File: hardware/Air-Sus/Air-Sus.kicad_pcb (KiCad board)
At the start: 2 copper layers, 1 part, among them U1 BME280

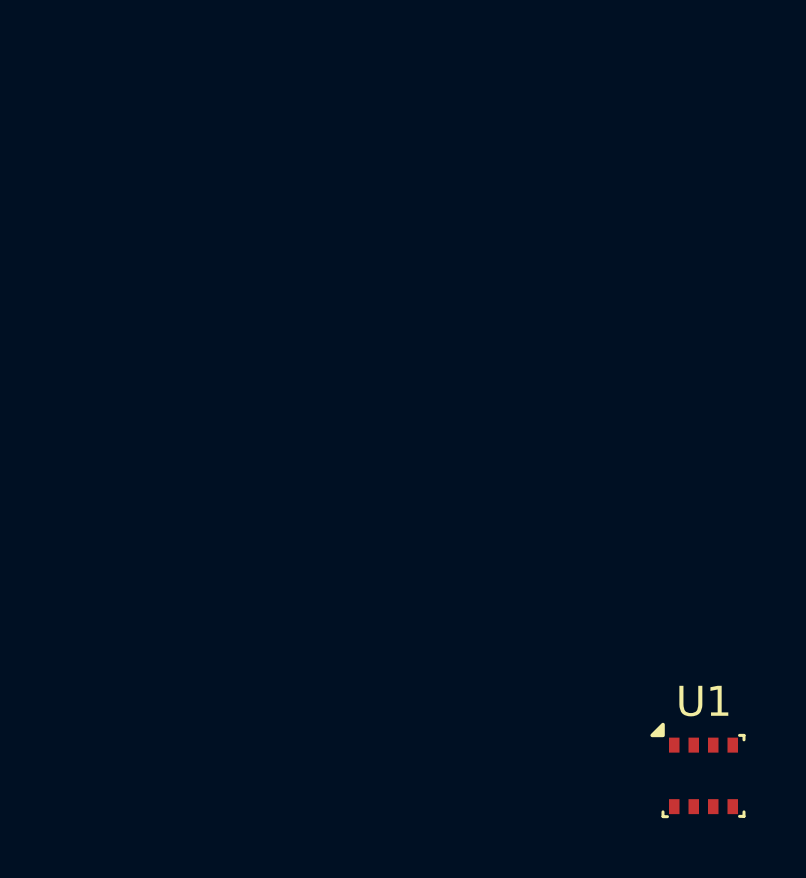
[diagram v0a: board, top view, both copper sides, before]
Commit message: added op-amp, finished footprints, new connector, fuse, ldo
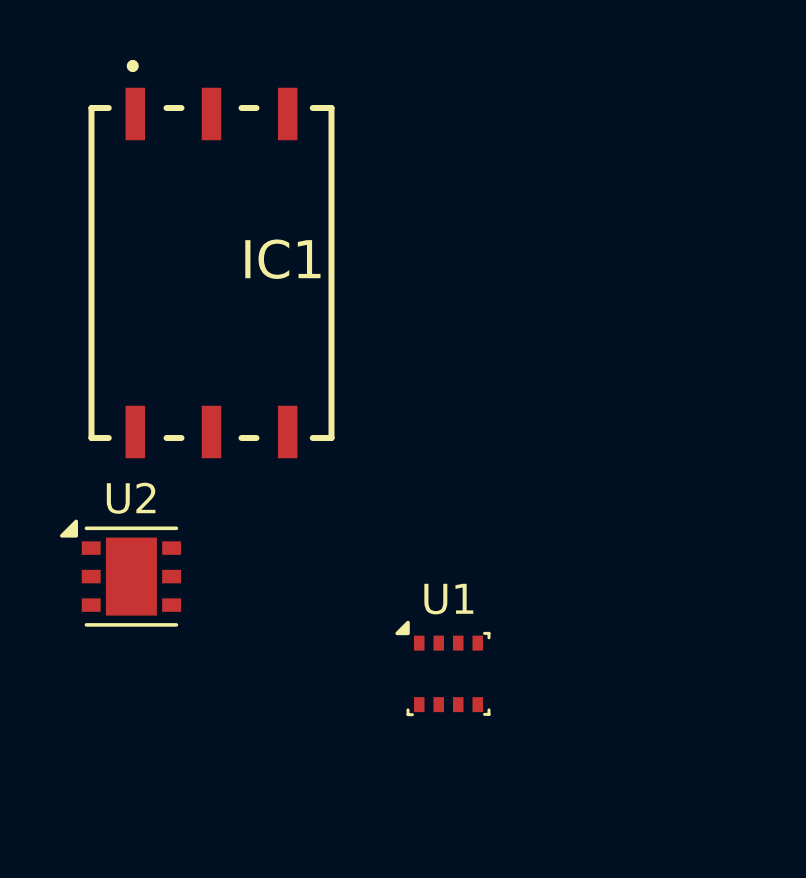
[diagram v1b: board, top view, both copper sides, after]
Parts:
- added IC1: ABPMRRV060MG2A3, footprints:ABPMRRV060MG2A3, F.Cu at (103.0, 69.6)
- added U2: LDO40LPURY, Package_DFN_QFN:DFN-6-1EP_3x3mm_P0.95mm_EP1.7x2.6mm, F.Cu at (100.4, 79.7)
- moved U1 9.15 mm to (110.9, 83.0)

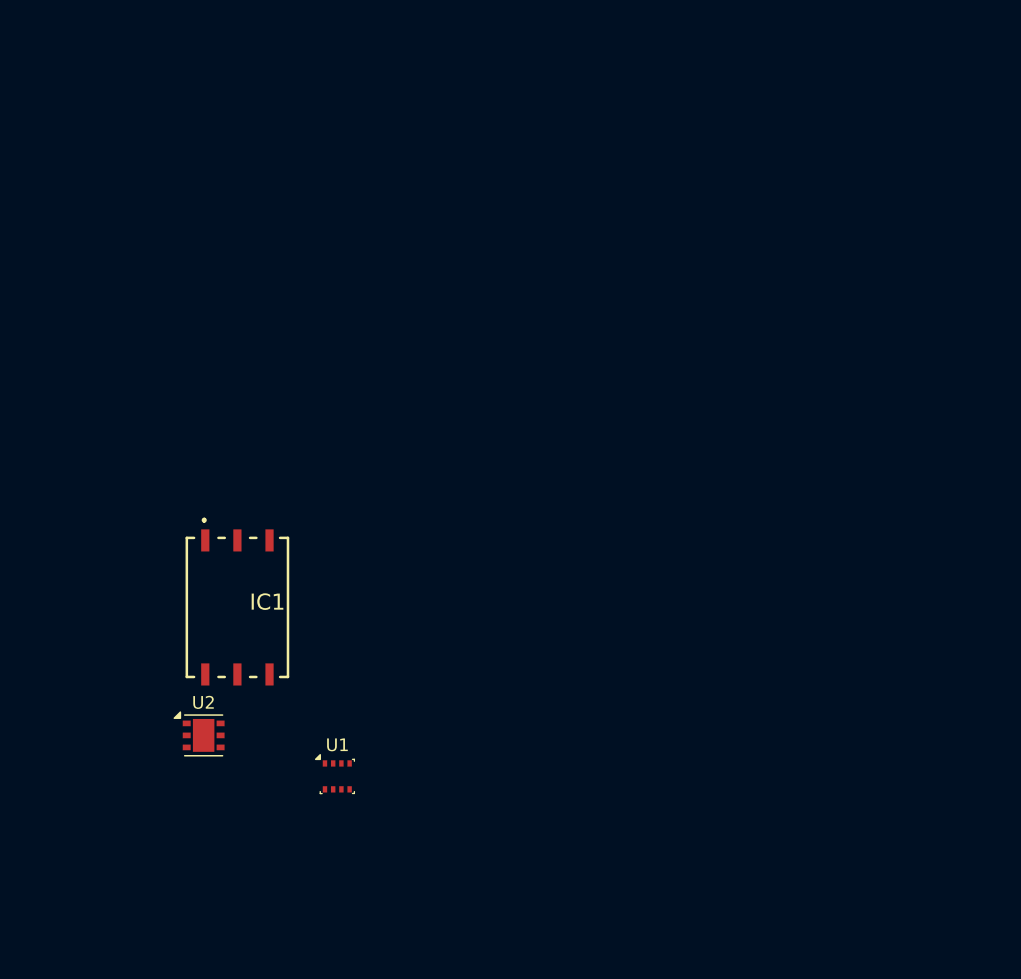
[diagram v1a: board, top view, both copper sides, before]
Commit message: added configurable options for board type/connector, cubemx ioc, nanofit for ir rideheight, added part numbers, etc.
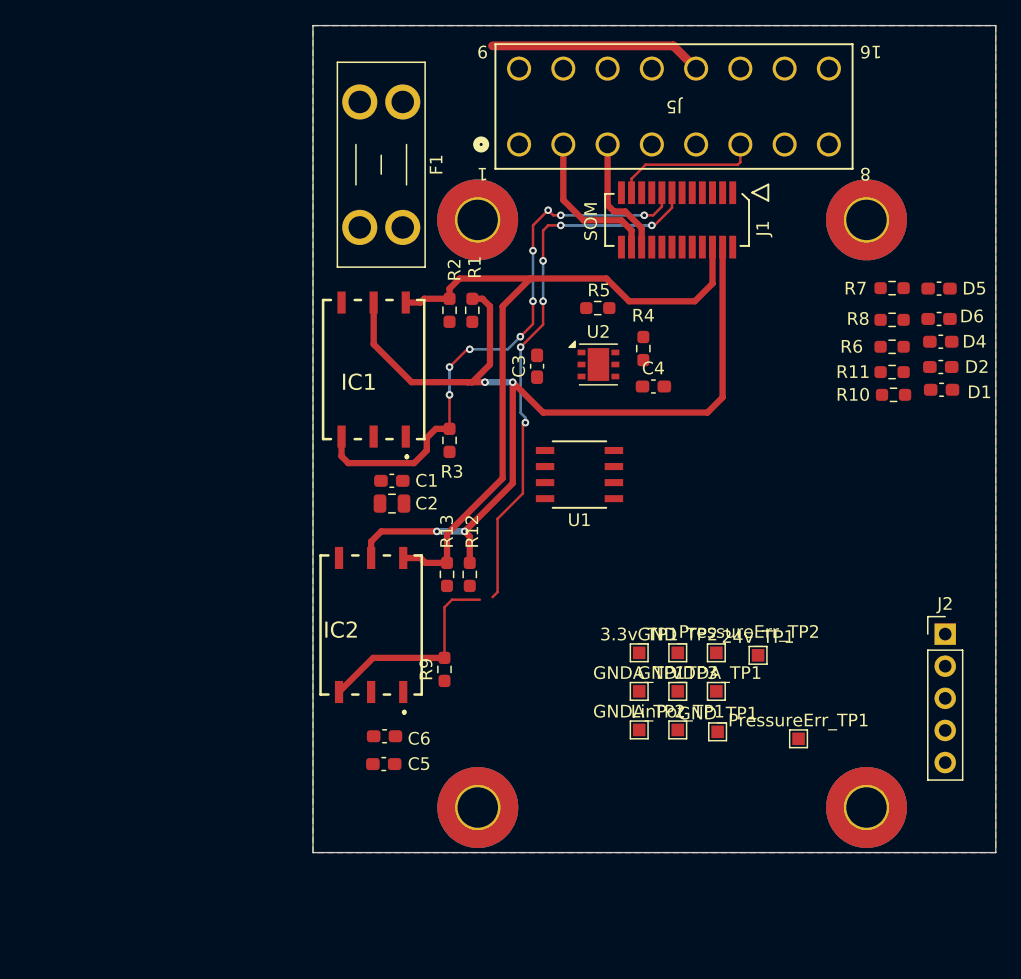
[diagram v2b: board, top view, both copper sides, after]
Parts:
- added 24v_TP1: TestPoint, TestPoint:TestPoint_Pad_1.0x1.0mm, F.Cu at (144.2, 73.4)
- added 3.3v_TP1: TestPoint, TestPoint:TestPoint_Pad_1.0x1.0mm, F.Cu at (134.8, 73.2)
- added C1: 0.1uF, Capacitor_SMD:C_0603_1608Metric_Pad1.08x0.95mm_HandSolder, F.Cu at (115.2, 59.6)
- added C2: 10uf, Capacitor_SMD:C_0805_2012Metric, F.Cu at (115.2, 61.4)
- added C3: 1uF, Capacitor_SMD:C_0603_1608Metric_Pad1.08x0.95mm_HandSolder, F.Cu at (126.7, 50.5)
- added C4: 1uF, Capacitor_SMD:C_0603_1608Metric_Pad1.08x0.95mm_HandSolder, F.Cu at (135.9, 52.1)
- added C5: 10uf, Capacitor_SMD:C_0603_1608Metric_Pad1.08x0.95mm_HandSolder, F.Cu at (114.6, 82.0)
- added C6: 0.1uF, Capacitor_SMD:C_0603_1608Metric_Pad1.08x0.95mm_HandSolder, F.Cu at (114.7, 79.8)
- added D1: LED, Capacitor_SMD:C_0603_1608Metric_Pad1.08x0.95mm_HandSolder, F.Cu at (158.7, 52.4)
- added D2: LED, Capacitor_SMD:C_0603_1608Metric_Pad1.08x0.95mm_HandSolder, F.Cu at (158.7, 50.6)
- added D4: LED, Capacitor_SMD:C_0603_1608Metric_Pad1.08x0.95mm_HandSolder, F.Cu at (158.7, 48.6)
- added D5: LED, Capacitor_SMD:C_0603_1608Metric_Pad1.08x0.95mm_HandSolder, F.Cu at (158.5, 44.4)
- added D6: LED, Capacitor_SMD:C_0603_1608Metric_Pad1.08x0.95mm_HandSolder, F.Cu at (158.5, 46.8)
- added F1: 500mA, Fuse:Fuseholder_Blade_Mini_Keystone_3568, F.Cu at (116.1, 29.6)
- added GNDA_TP1: TestPoint, TestPoint:TestPoint_Pad_1.0x1.0mm, F.Cu at (134.8, 76.2)
- added GNDA_TP2: TestPoint, TestPoint:TestPoint_Pad_1.0x1.0mm, F.Cu at (134.8, 79.3)
- added GND_TP1: TestPoint, TestPoint:TestPoint_Pad_1.0x1.0mm, F.Cu at (141.0, 79.5)
- added GND_TP2: TestPoint, TestPoint:TestPoint_Pad_1.0x1.0mm, F.Cu at (137.8, 73.2)
- added GND_TP3: TestPoint, TestPoint:TestPoint_Pad_1.0x1.0mm, F.Cu at (137.8, 76.2)
- added IC2: ABPMRRV060MG2A3, footprints:ABPMRRV060MG2A3, F.Cu at (113.6, 71.0)
- added J1: 53307-2471, UTSVT_Connectors:PeripheralSOM, F.Cu at (137.8, 39.0)
- added J2: Conn_01x05, Connector_PinHeader_2.54mm:PinHeader_1x05_P2.54mm_Vertical, F.Cu at (159.0, 71.7)
- added J5: MX150_02x08_Vertical, UTSVT_Connectors:CONN16_0757575481_MOL, F.Cu at (137.5, 30.0)
- added LinPot_TP1: TestPoint, TestPoint:TestPoint_Pad_1.0x1.0mm, F.Cu at (137.8, 79.3)
- added PressureErr_TP1: TestPoint, TestPoint:TestPoint_Pad_1.0x1.0mm, F.Cu at (147.4, 80.0)
- added PressureErr_TP2: TestPoint, TestPoint:TestPoint_Pad_1.0x1.0mm, F.Cu at (140.9, 73.2)
- added R1: 4.7k, Resistor_SMD:R_0603_1608Metric_Pad0.98x0.95mm_HandSolder, F.Cu at (121.6, 46.1)
- added R10: 100, Resistor_SMD:R_0603_1608Metric_Pad0.98x0.95mm_HandSolder, F.Cu at (154.9, 52.8)
- added R11: 100, Resistor_SMD:R_0603_1608Metric_Pad0.98x0.95mm_HandSolder, F.Cu at (154.8, 51.0)
- added R12: 4.7k, Resistor_SMD:R_0603_1608Metric_Pad0.98x0.95mm_HandSolder, F.Cu at (121.4, 67.0)
- added R13: 4.7k, Resistor_SMD:R_0603_1608Metric_Pad0.98x0.95mm_HandSolder, F.Cu at (119.6, 67.0)
- added R2: 4.7k, Resistor_SMD:R_0603_1608Metric_Pad0.98x0.95mm_HandSolder, F.Cu at (119.8, 46.1)
- added R3: 4.7k, Resistor_SMD:R_0603_1608Metric_Pad0.98x0.95mm_HandSolder, F.Cu at (119.8, 56.4)
- added R4: 10k, Resistor_SMD:R_0603_1608Metric_Pad0.98x0.95mm_HandSolder, F.Cu at (135.1, 49.1)
- added R5: 17.5k, Resistor_SMD:R_0603_1608Metric_Pad0.98x0.95mm_HandSolder, F.Cu at (131.5, 45.9)
- added R6: 100, Resistor_SMD:R_0603_1608Metric_Pad0.98x0.95mm_HandSolder, F.Cu at (154.8, 49.0)
- added R7: 100, Resistor_SMD:R_0603_1608Metric_Pad0.98x0.95mm_HandSolder, F.Cu at (154.8, 44.4)
- added R8: 100, Resistor_SMD:R_0603_1608Metric_Pad0.98x0.95mm_HandSolder, F.Cu at (154.8, 46.9)
- added R9: 4.7k, Resistor_SMD:R_0603_1608Metric_Pad0.98x0.95mm_HandSolder, F.Cu at (119.4, 74.5)
- added VDDA_TP1: TestPoint, TestPoint:TestPoint_Pad_1.0x1.0mm, F.Cu at (140.9, 76.2)
- U1: value BME280 -> Opamp_Dual; footprint Package_LGA:Bosch_LGA-8_2.5x2.5mm_P0.65mm_ClockwisePinNumbering -> TLV900QDRQ1:SOIC8_D_TEX
- moved U2 42.8 mm to (131.6, 50.4)
- moved U1 30.6 mm to (130.1, 59.1)
- moved IC1 21.7 mm to (113.8, 50.8), turned to 180 degrees
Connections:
- IC1 pad 3: /pressure_err -> /pressure_err1
- U1 pad 1: GND -> /linpot_norm
- U1 pad 2: +3.3V -> /linpot_norm
- U1 pad 3: /SDA -> /linpot_out
- U1 pad 4: /SCL -> GNDA
- U1 pad 5: GND -> unconnected-(U1B-+-Pad5)
- U1 pad 6: +3.3V -> unconnected-(U1B---Pad6)
- U1 pad 7: GND -> unconnected-(U1-Pad7)
- U1 pad 8: +3.3V -> VDDA
- U2 pad 4: +3.3V -> Net-(U2-Vout)
- U2 pad 5: +3.3V -> Net-(U2-Vout)
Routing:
- net /SDA: track 0.00 -> 79.2 mm, vias 0 -> 4
- net /pressure_err2: track 0.00 -> 59.6 mm, vias 0 -> 6
- net /SCL: track 0.00 -> 58.6 mm
- net /pressure_err1: track 0.00 -> 45.0 mm, vias 0 -> 9
- net +3.3V: track 0.00 -> 16.8 mm
- net /CAN_H: track 0.00 -> 12.1 mm
- net /SDA2: track 0.00 -> 11.6 mm
- net /CAN_L: track 0.00 -> 9.75 mm
- added copper zone on F.Cu, net +3.3V
- added copper zone on B.Cu, net GND
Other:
- board outline added: 54 x 65.4 mm

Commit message: air-sus layout check e Please enter the commit message for your changes. Lines starting
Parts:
- removed D1, D2, D4, D5, D6: LED, Capacitor_SMD:C_0603_1608Metric_Pad1.08x0.95mm_HandSolder
- removed R10, R11, R6, R7, R8: 100, Resistor_SMD:R_0603_1608Metric_Pad0.98x0.95mm_HandSolder
- added C7: 0.1uF, Capacitor_SMD:C_0603_1608Metric_Pad1.08x0.95mm_HandSolder, F.Cu at (125.4, 48.5)
- added D10: LED, Capacitor_SMD:C_0603_1608Metric_Pad1.08x0.95mm_HandSolder, F.Cu at (136.2, 61.4)
- added D3: LED, Capacitor_SMD:C_0603_1608Metric_Pad1.08x0.95mm_HandSolder, F.Cu at (136.2, 55.4)
- added D7: LED, Capacitor_SMD:C_0603_1608Metric_Pad1.08x0.95mm_HandSolder, F.Cu at (136.2, 49.6)
- added D8: LED, Capacitor_SMD:C_0603_1608Metric_Pad1.08x0.95mm_HandSolder, F.Cu at (136.2, 52.6)
- added D9: LED, Capacitor_SMD:C_0603_1608Metric_Pad1.08x0.95mm_HandSolder, F.Cu at (136.2, 58.6)
- added J4: MX150_02x06_Vertical, UTSVT_Connectors:MX150_02x06_Vertical, B.Cu at (108.1, 69.2)
- added R14: 1k, Resistor_SMD:R_0603_1608Metric_Pad0.98x0.95mm_HandSolder, F.Cu at (132.8, 55.4)
- added R15: 1k, Resistor_SMD:R_0603_1608Metric_Pad0.98x0.95mm_HandSolder, F.Cu at (132.9, 49.6)
- added R16: 1k, Resistor_SMD:R_0603_1608Metric_Pad0.98x0.95mm_HandSolder, F.Cu at (132.8, 52.6)
- added R17: 1k, Resistor_SMD:R_0603_1608Metric_Pad0.98x0.95mm_HandSolder, F.Cu at (132.9, 58.6)
- added R18: 1k, Resistor_SMD:R_0603_1608Metric_Pad0.98x0.95mm_HandSolder, F.Cu at (132.8, 61.4)
- added R38: 2.49k, Resistor_SMD:R_0603_1608Metric_Pad0.98x0.95mm_HandSolder, F.Cu at (98.9, 56.2)
- added RN1: YC324-JK-070RL, 4pinRes:YC324JK07220RL, F.Cu at (119.6, 76.5)
- added RN2: YC324-JK-070RL, 4pinRes:YC324JK07220RL, F.Cu at (112.5, 88.3)
- added RN4: YC324-JK-070RL, 4pinRes:YC324JK07220RL, F.Cu at (112.5, 76.5)
- added RN5: YC324-JK-070RL, 4pinRes:YC324JK07220RL, F.Cu at (112.5, 82.4)
- added RN6: YC324-JK-070RL, 4pinRes:YC324JK07220RL, F.Cu at (119.6, 82.4)
- added RN7: YC324-JK-070RL, 4pinRes:YC324JK07220RL, F.Cu at (119.6, 88.3)
- J5: value MX150_02x08_Vertical -> Conn_01x06; footprint UTSVT_Connectors:CONN16_0757575481_MOL -> Connector_Molex:Molex_Nano-Fit_105310-xx06_2x03_P2.50mm_Vertical
- R5: value 17.5k -> 15k
- moved 24v_TP1 66.5 mm to (91.2, 33.1)
- moved GND_TP1 65.9 mm to (94.1, 33.1)
- moved VDDA_TP1 60.4 mm to (91.3, 41.7)
- moved PressureErr_TP1 59.6 mm to (89.0, 68.0)
- moved LinPot_TP1 59.3 mm to (100.5, 33.1)
- moved GND_TP2 56.5 mm to (94.0, 37.5)
- moved 3.3v_TP1 56.2 mm to (91.5, 37.5)
- moved GNDA_TP2 55.9 mm to (103.2, 33.2)
- moved PressureErr_TP2 55.2 mm to (88.8, 91.3)
- moved GND_TP3 53.8 mm to (100.5, 37.5)
- moved GNDA_TP1 53.5 mm to (93.8, 41.8)
- moved C4 37.2 mm to (100.5, 63.7), turned to 90 degrees
- moved R9 33.6 mm to (88.8, 88.5), turned to -90 degrees
- moved R4 33.0 mm to (102.9, 56.2)
- moved R5 32.7 mm to (100.5, 56.2), turned to 90 degrees
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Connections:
- net /SCL2 renamed SCL2
- J1 pad 12: /diff_status -> diff_status
- J1 pad 14: /Temp_status -> Temp_status
- J1 pad 16: /ir_status -> ir_status
- J1 pad 20: /CAN_L -> CAN_L
- J1 pad 21: /SDA2 -> SDA2
- J1 pad 22: /CAN_H -> CAN_H
- J1 pad 9: /linpot12_out -> /linpot_norm
- J2 pad 3: /SDA2 -> SDA2
- J5 pad 1: +24V -> unconnected-(J5-Pin_1-Pad1)
- J5 pad 2: /CAN_H -> GND
- J5 pad 3: /CAN_L -> SDA2
- J5 pad 4: +24V -> +3.3V
- J5 pad 6: /SDA2 -> /IR_STAT
- LinPot_TP1 pad 1: /linpot12_out -> linpot_out
- R5 pad 2: GND -> Net-(R38-Pad1)
- U1 pad 3: /linpot_out -> linpot_out
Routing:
- net +24V: track 0.00 -> 130.5 mm, vias 0 -> 15
- net SCL2: track 0.00 -> 129.6 mm, vias 0 -> 12
- net GNDA: track 0.00 -> 99.8 mm, vias 0 -> 14
- net SDA2: track 0.00 -> 99.7 mm, vias 0 -> 6
- net linpot_out: track 0.00 -> 77.5 mm, vias 0 -> 5
- net /SCL: track 58.6 -> 127.6 mm, vias 0 -> 15
- net CAN_L: track 0.00 -> 66.2 mm, vias 0 -> 3
- net CAN_H: track 0.00 -> 62.5 mm, vias 0 -> 2
- net GND: track 0.00 -> 57.8 mm, vias 0 -> 28
- net /mx150Connector/Gen_8: track 0.00 -> 49.4 mm, vias 0 -> 7
- net /SDA: track 79.2 -> 128.0 mm, vias 4 -> 12
- net Net-(U2-Vout): track 0.00 -> 42.4 mm, vias 0 -> 2
- net /3.3MCU: track 0.00 -> 41.3 mm, vias 0 -> 4
- net Temp_status: track 0.00 -> 34.8 mm, vias 0 -> 6
- net /linpot_norm: track 0.00 -> 34.5 mm, vias 0 -> 4
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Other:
- board size 54 x 65.4 mm -> 51.6 x 65.3 mm
- board text added: "*"
- board text added: "1 7"

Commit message: finished rev a layout for all 3 boards + added cubemx file
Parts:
- removed C5: 10uf, Capacitor_SMD:C_0603_1608Metric_Pad1.08x0.95mm_HandSolder
- removed C6: 0.1uF, Capacitor_SMD:C_0603_1608Metric_Pad1.08x0.95mm_HandSolder
- removed IC2: ABPMRRV060MG2A3, footprints:ABPMRRV060MG2A3
- removed R12, R13, R9: 4.7k, Resistor_SMD:R_0603_1608Metric_Pad0.98x0.95mm_HandSolder
- added C8: 10uf, Capacitor_SMD:C_0805_2012Metric, F.Cu at (96.2, 94.9)
- added C9: 0.1uF, Capacitor_SMD:C_0603_1608Metric_Pad1.08x0.95mm_HandSolder, F.Cu at (96.3, 93.1)
- added G***: LOGO, UTSVT_Logos:UTSVT_Logo_Symbol, F.Cu at (102.7, 83.6)
- added G***: LHRs_LOGO, UTSVT_Logos:LHRs_LOGO, F.Cu at (100.6, 37.5)
- added IC3: ABPMRRV060MG2A3, footprints:ABPMRRV060MG2A3, F.Cu at (95.0, 84.3)
- added R6: 4.7k, Resistor_SMD:R_0603_1608Metric_Pad0.98x0.95mm_HandSolder, F.Cu at (92.5, 94.1)
- added R7: 4.7k, Resistor_SMD:R_0603_1608Metric_Pad0.98x0.95mm_HandSolder, F.Cu at (94.9, 75.5)
- added R8: 4.7k, Resistor_SMD:R_0603_1608Metric_Pad0.98x0.95mm_HandSolder, F.Cu at (97.7, 75.5)
- 24v_TP1, 3.3v_TP1, GNDA_TP1, GNDA_TP2, GND_TP1, GND_TP2, GND_TP3, LinPot_TP1, PressureErr_TP1, PressureErr_TP2, VDDA_TP1: moved to B.Cu
- moved GND_TP3 61.4 mm to (125.1, 93.8), turned to 180 degrees
- moved GNDA_TP2 61.1 mm to (111.1, 93.8), turned to 180 degrees
- moved LinPot_TP1 60.5 mm to (133.1, 84.2), turned to 180 degrees
- moved GNDA_TP1 57.5 mm to (118.2, 93.8), turned to 180 degrees
- moved 24v_TP1 40.4 mm to (121.6, 59.8)
- moved GND_TP2 39.5 mm to (103.8, 75.8), turned to 180 degrees
- moved 3.3v_TP1 39.5 mm to (101.4, 75.7), turned to 180 degrees
- moved PressureErr_TP1 34.5 mm to (106.3, 38.1), turned to 180 degrees
- moved GND_TP1 33.7 mm to (119.3, 55.6), turned to 180 degrees
- moved PressureErr_TP2 27.1 mm to (101.6, 67.5), turned to 180 degrees
- moved VDDA_TP1 24.3 mm to (113.1, 52.5), turned to 180 degrees
- moved R38 7.36 mm to (105.5, 53.0), turned to 180 degrees
- moved RN7 6.71 mm to (121.8, 81.9), turned to 0 degrees
- moved RN2 6.69 mm to (114.6, 81.9)
- moved F1 6.14 mm to (114.2, 36.5), turned to 0 degrees
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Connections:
- net CAN_H renamed /CAN_H
- net CAN_L renamed /CAN_L
- net diff_status renamed /diff_status
- net ir_status renamed /ir_status
- C1 pad 1: +3.3V -> +3.3V MCU
- C2 pad 1: +3.3V -> +3.3V MCU
- IC1 pad 2: +3.3V -> +3.3V MCU
- J1 pad 11: /IR_STAT -> /pressure_err2
- J1 pad 13: /pressure_err2 -> unconnected-(J1-ADC1_IN10-Pad13)
- J1 pad 14: Temp_status -> /SDA2
- J1 pad 15: /pressure_err1 -> unconnected-(J1-ADC1_IN11-Pad15)
- J1 pad 18: SCL2 -> /SCL2
- J1 pad 19: unconnected-(J1-SPI1_NSS-Pad19) -> /IR_INTER
- J1 pad 2: /3.3MCU -> +3.3V MCU
- J1 pad 21: SDA2 -> unconnected-(J1-SPI1_MISO-Pad21)
- J1 pad 23: unconnected-(J1-SPI1_SCK-Pad23) -> /pressure_err1
- J1 pad 7: unconnected-(J1-OPAMP1_VINP-Pad7) -> /Temp_status
- J2 pad 3: SDA2 -> /SDA2
- J2 pad 4: SCL2 -> /SCL2
- J5 pad 3: SDA2 -> /SDA
- J5 pad 5: SCL2 -> /SCL
- J5 pad 6: /IR_STAT -> /IR_INTER
- R18 pad 1: Temp_status -> /Temp_status
- RN1 pad 5: SDA2 -> /SCL2
- RN1 pad 7: SCL2 -> /SDA2
- RN4 pad 6: SDA2 -> /SDA
- RN4 pad 7: SCL2 -> /SCL
- U2 pad 2: /3.3MCU -> /24v_out
- VDDA_TP1 pad 1: +VDDA -> VDDA
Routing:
- net SCL2: track 129.6 -> 0.00 mm, vias 12 -> 0
- net GND: track 57.8 -> 164.6 mm, vias 28 -> 30
- net /SDA2: track 0.00 -> 100.4 mm, vias 0 -> 7
- net SDA2: track 99.7 -> 0.00 mm, vias 6 -> 0
- net /SCL2: track 0.00 -> 97.8 mm, vias 0 -> 9
- net +3.3V MCU: track 0.00 -> 72.1 mm, vias 0 -> 8
- net +24V: track 130.5 -> 77.7 mm, vias 15 -> 9
- net +3.3V: track 0.01 -> 45.4 mm, vias 0 -> 15
- net /3.3MCU: track 41.3 -> 0.00 mm, vias 4 -> 0
- net GNDA: track 99.8 -> 64.5 mm, vias 14 -> 7
- net Temp_status: track 34.8 -> 0.00 mm, vias 6 -> 0
- net linpot_out: track 77.5 -> 44.0 mm, vias 5 -> 6
- net /Temp_status: track 0.00 -> 29.7 mm, vias 0 -> 2
- net /IR_INTER: track 0.00 -> 28.1 mm, vias 0 -> 2
- net /IR_STAT: track 27.1 -> 0.00 mm
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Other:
- board size 51.6 x 65.3 mm -> 50.1 x 63.6 mm
- board text removed: "*"
- board text removed: "1 7"
